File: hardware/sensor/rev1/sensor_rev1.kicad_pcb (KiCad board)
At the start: 2 copper layers, 28.9 x 64.4 mm, 58 parts, among them IC1 STM8L051F3P6, IC2 CC1101RGPR, J1 22-28-4044, J2 M20-9770342, Y1 NX3225GA-26.000M-STD-CRG-2

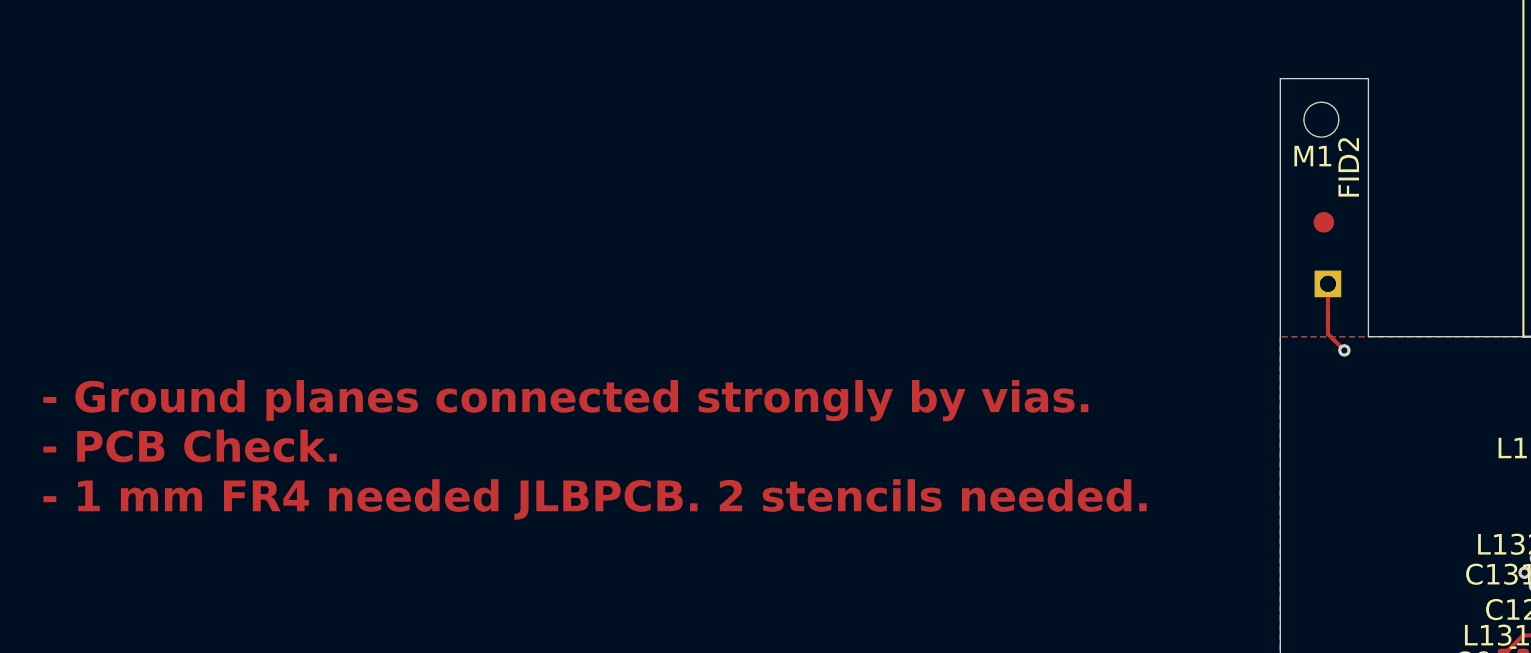
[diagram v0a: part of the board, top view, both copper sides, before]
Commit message: EG-50 Components labels fixed.
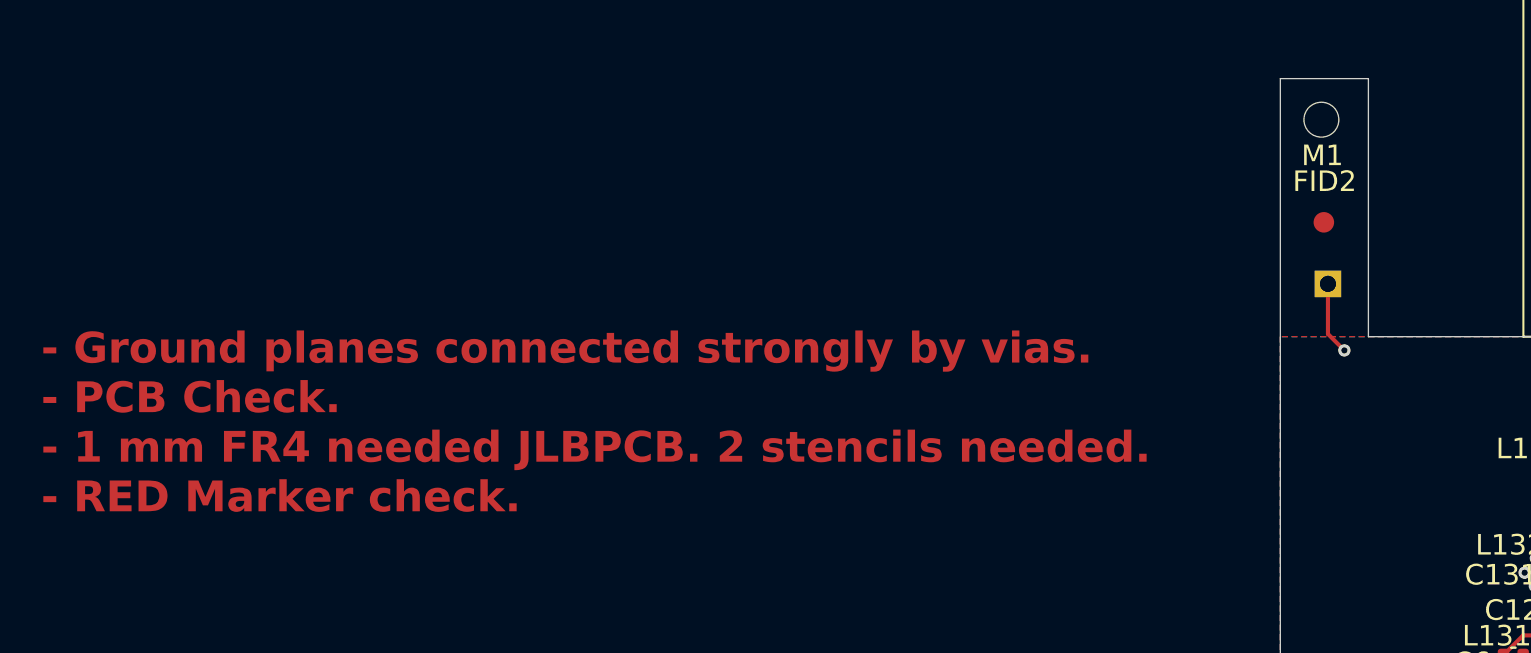
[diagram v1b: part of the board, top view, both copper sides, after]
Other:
- board text added: "- Ground planes connected strongly by vias. - PCB Check. - 1 mm FR4 needed JLBPCB. 2 stencils needed. - RED Marker check."
- board text removed: "- Ground planes connected strongly by vias. - PCB Check. - 1 mm FR4 needed JLBPCB. 2 stencils needed."
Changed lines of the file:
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@@
 		(tags "fiducial")
 		(property "Reference" "FID2"
-			(at 1.25 -2.68 90)
+			(at 0.04 -1.99 180)
 			(layer "F.SilkS")
 			(effects
@@
 		(at 222 92)
 		(property "Reference" "M1"
-			(at -0.42 1.81 0)
+			(at 0.05 1.75 0)
 			(unlocked yes)
 			(layer "F.SilkS")
@@
 		(layer "Edge.Cuts")
 	)
-	(gr_text "- Ground planes connected strongly by vias.\n- PCB Check.\n- 1 mm FR4 needed JLBPCB. 2 stencils needed.\n"
+	(gr_text "- Ground planes connected strongly by vias.\n- PCB Check.\n- 1 mm FR4 needed JLBPCB. 2 stencils needed.\n- RED Marker check.\n"
 		(at 159.63 111.26 0)
 		(layer "F.Cu")
@@
 		(min_thickness 0.25)
 		(filled_areas_thickness no)
-		(fill
+		(fill yes
 			(thermal_gap 0.5)
 			(thermal_bridge_width 0.5)
@@
 		(min_thickness 0.25)
 		(filled_areas_thickness no)
-		(fill
+		(fill yes
 			(thermal_gap 0.5)
 			(thermal_bridge_width 0.5)

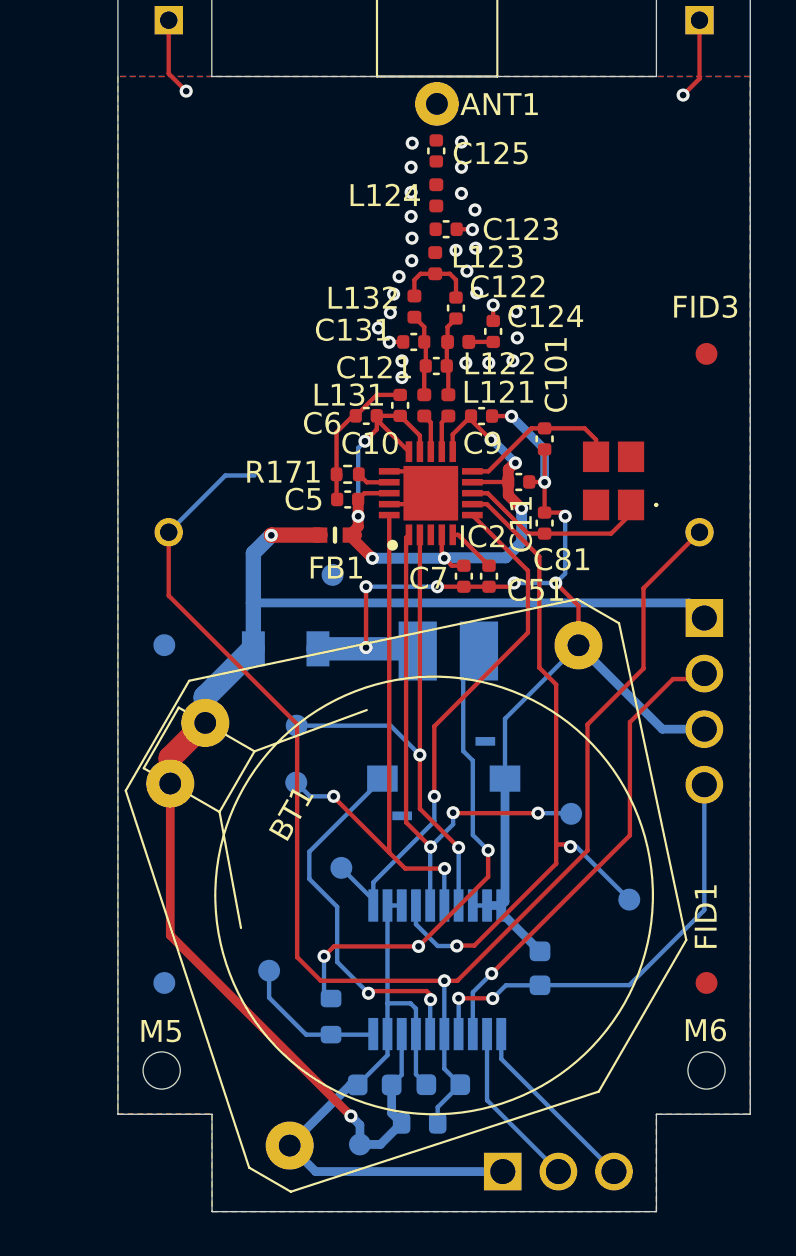
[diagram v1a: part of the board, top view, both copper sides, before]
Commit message: EG-50 Placed vias in the non-RF part.
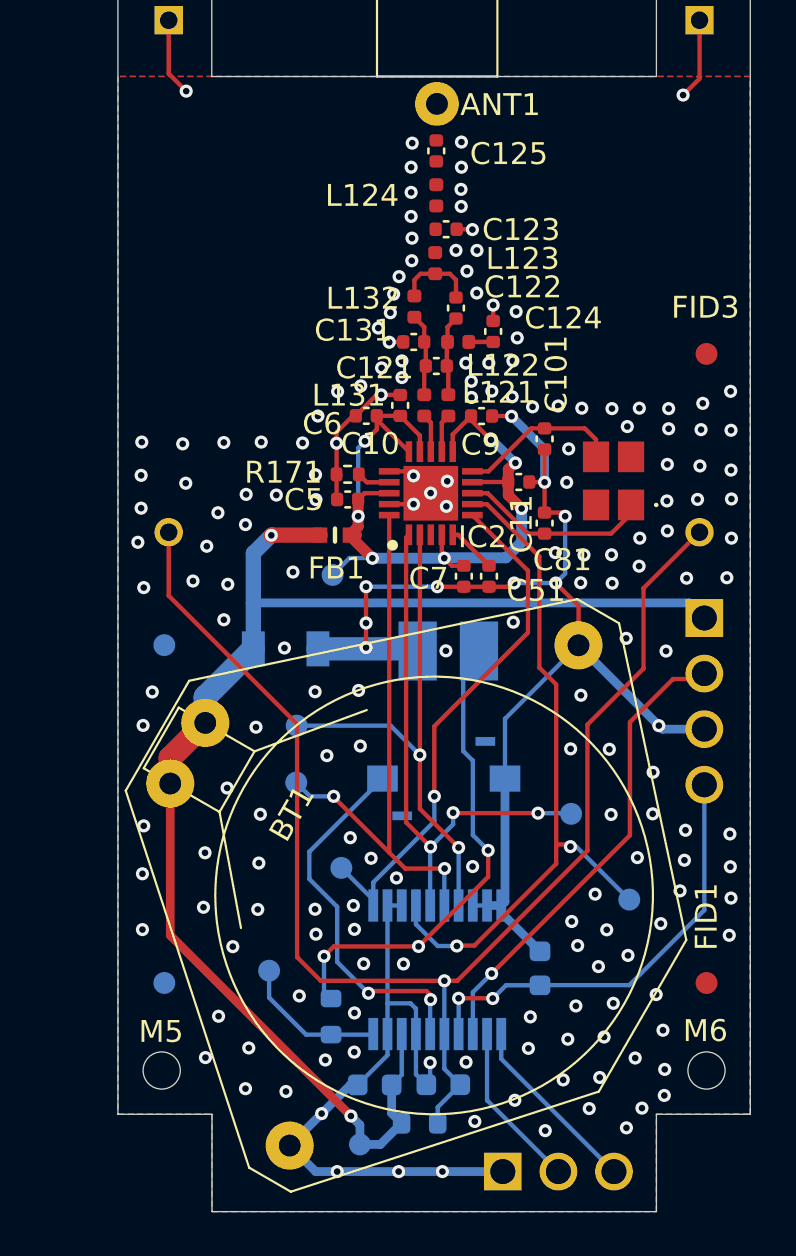
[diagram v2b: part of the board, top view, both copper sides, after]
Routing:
- net REED: track 66.9 -> 61.9 mm
- net RF_VDD: track 35.6 -> 37.8 mm
- net GND: track 108.3 -> 109.4 mm, vias 38 -> 194

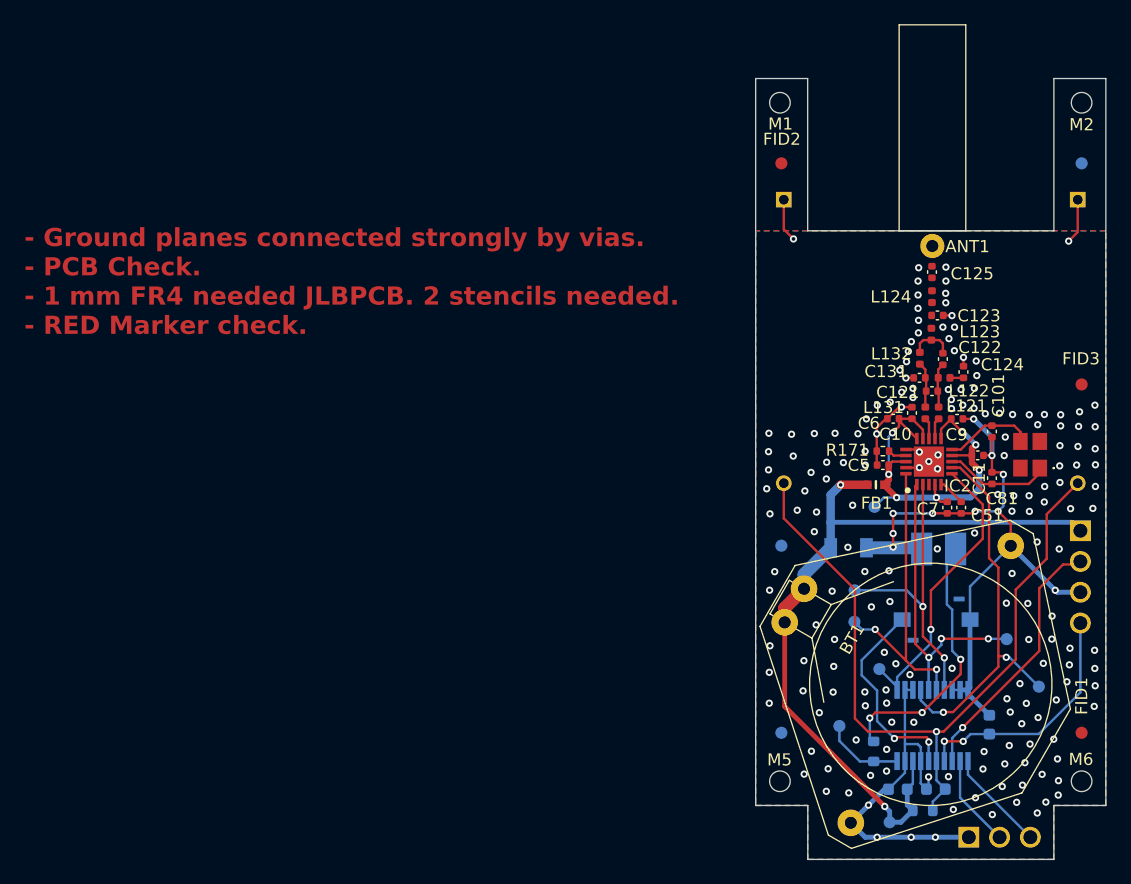
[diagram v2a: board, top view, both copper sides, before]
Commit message: EG-50 DRC errors fixed. Only warnings.
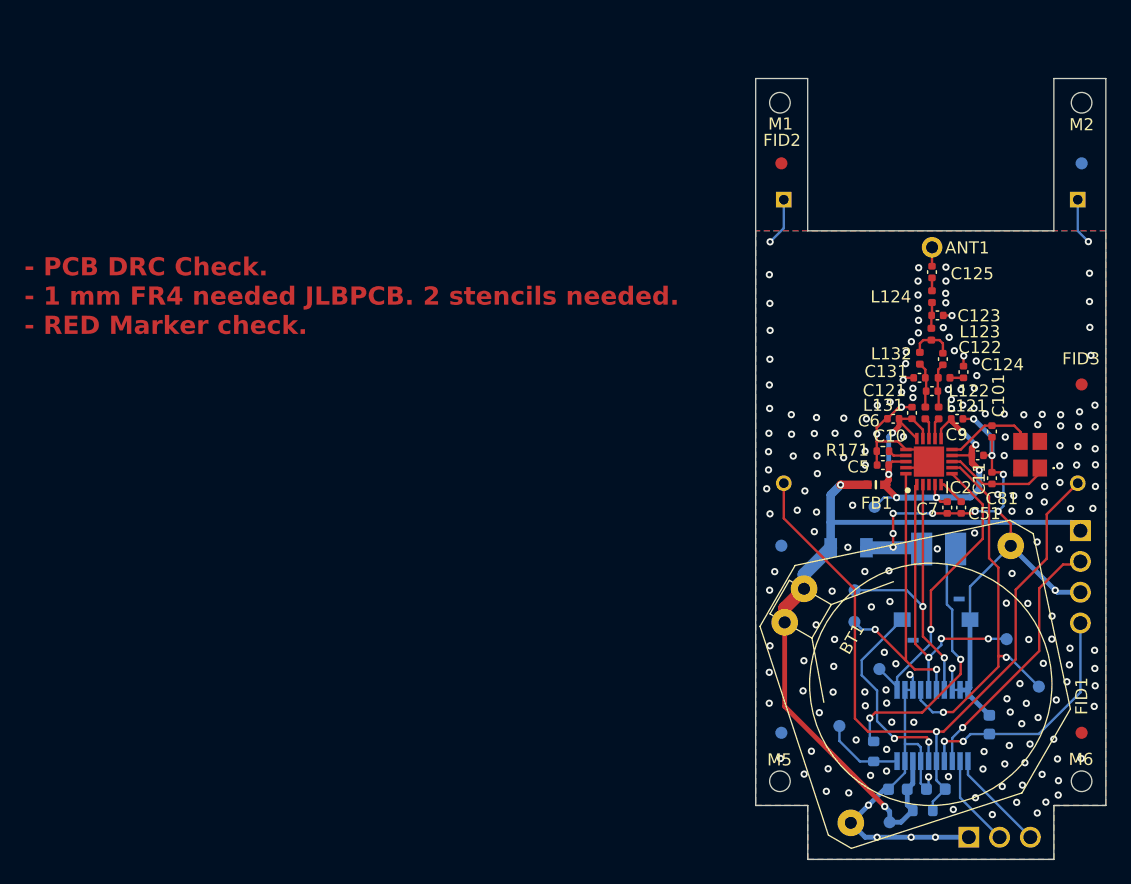
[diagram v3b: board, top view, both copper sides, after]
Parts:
- moved ANT1 0.11 mm to (234.5, 105.7)
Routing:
- net GND: track 109.4 -> 117.5 mm, vias 194 -> 201
- net Net-(C123-Pad2): track 0.00 -> 2.15 mm
- net Net-(ANT1-ANT): track 0.00 -> 1.61 mm
- net Net-(C125-Pad1): track 0.00 -> 1.06 mm
- net Net-(LED1-A): vias 3 -> 2
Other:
- board text added: "- PCB DRC Check. - 1 mm FR4 needed JLBPCB. 2 stencils needed. - RED Marker check."
- board text removed: "- Ground planes connected strongly by vias. - PCB Check. - 1 mm FR4 needed JLBPCB. 2 stencils needed. - RED Marker check."

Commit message: EG-50 Only warings on CR2032 battery holder.
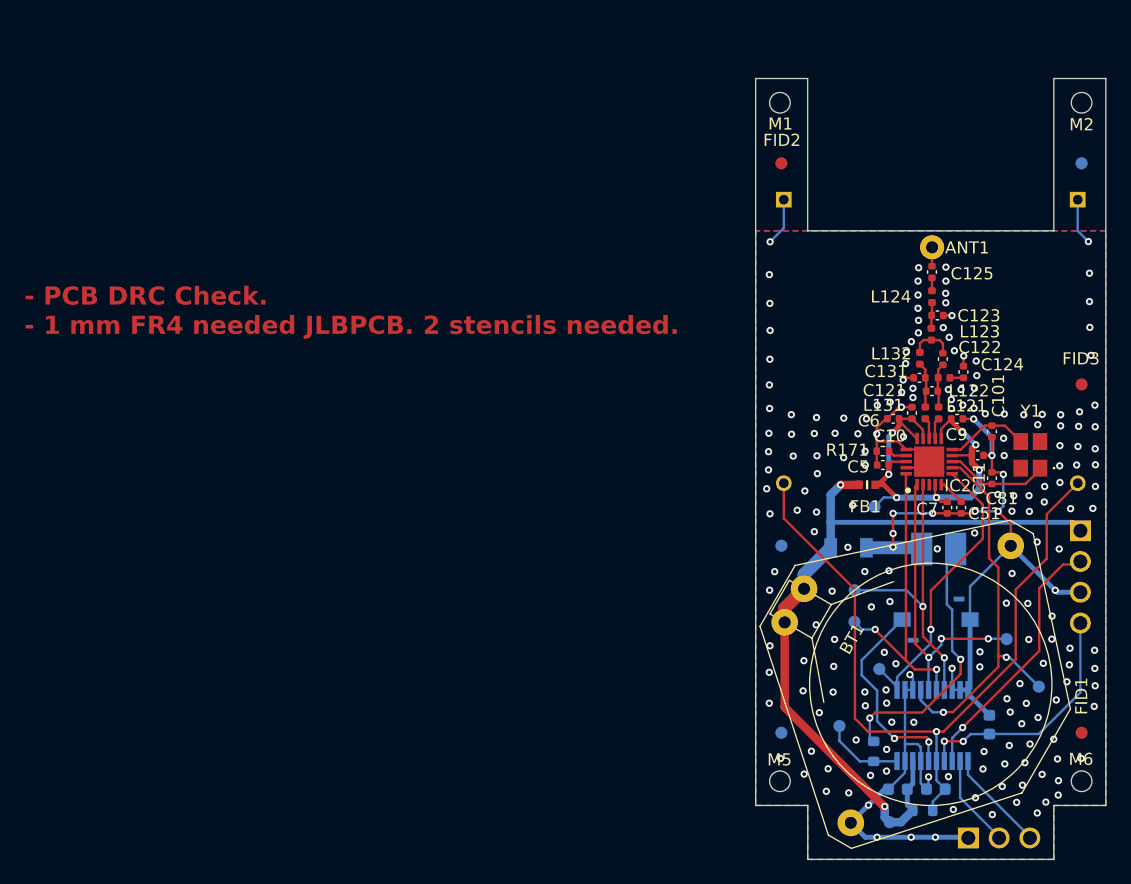
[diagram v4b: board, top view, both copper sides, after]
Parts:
- moved FB1 0.72 mm to (229.2, 123.5), turned to 180 degrees
- moved J2 0.07 mm to (237.6, 152.7)
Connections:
- FB1 pad 1: VDD -> RF_VDD
- FB1 pad 2: RF_VDD -> VDD
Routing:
- net RF_VDD: track 37.8 -> 38.6 mm
- net VDD: track 63.2 -> 62.6 mm
- net GND: vias 201 -> 203
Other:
- board text added: "- PCB DRC Check. - 1 mm FR4 needed JLBPCB. 2 stencils needed."
- board text removed: "- PCB DRC Check. - 1 mm FR4 needed JLBPCB. 2 stencils needed. - RED Marker check."

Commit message: EG-50 Fix the CR2032 battery holder footprint.
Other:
- board text added: "- 1 mm FR4 needed JLBPCB. 2 stencils needed."
- board text removed: "- PCB DRC Check. - 1 mm FR4 needed JLBPCB. 2 stencils needed."
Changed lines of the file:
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@@
 		(fp_line
 			(start -1.6 -14.4)
-			(end -1.6 -14.1)
+			(end -1.6 -14.3)
 			(stroke
 				(width 0.1)
@@
 		(fp_line
 			(start 1.6 -14.4)
-			(end 1.6 -14.1)
+			(end 1.6 -14.3)
 			(stroke
 				(width 0.1)
@@
 		(fp_line
 			(start -1.6 -10.4)
-			(end -1.6 -11.9)
+			(end -1.6 -11.7)
 			(stroke
 				(width 0.1)
@@
 		)
 		(fp_line
-			(start 1.6 -11.9)
+			(start 1.6 -11.7)
 			(end 1.6 -10.4)
 			(stroke
@@
 		)
 		(embedded_fonts no)
-		(model "${KIPRJMOD}/libraries/3dmodels/MyParts/GRM31CR61A107MEA8L.stp"
+		(model "GRM31CR61A107MEA8L.stp"
 			(offset
 				(xyz 0 0 0)
@@
 		)
 		(embedded_fonts no)
+		(model "${KIPRJMOD}/libraries/3dmodels/MyParts/M20-9770342.stp"
+			(offset
+				(xyz 0 0 0)
+			)
+			(scale
+				(xyz 1 1 1)
+			)
+			(rotate
+				(xyz 0 0 0)
+			)
+		)
 	)
 	(footprint "MyParts:PTS636SMG25JSMTRLFS"
@@
 		)
 		(embedded_fonts no)
-		(model "${KIPRJMOD}/libraries/3dmodels/MyParts/PTS636SMG25JSMTR_LFS.stp"
+		(model "PTS636SMG25JSMTR_LFS.stp"
 			(offset
 				(xyz 0 0 0)
@@
 		)
 		(embedded_fonts no)
-		(model "${KIPRJMOD}/libraries/3dmodels/MyParts/VLMS3000-GS08.stp"
+		(model "VLMS3000-GS08.stp"
 			(offset
 				(xyz 0 0 0)
@@
 		)
 		(embedded_fonts no)
-		(model "${KIPRJMOD}/libraries/3dmodels/MyParts/STM8L051F3P6.stp"
+		(model "STM8L051F3P6.stp"
 			(offset
 				(xyz 0 0 0)
@@
 		(layer "Edge.Cuts")
 	)
-	(gr_text "- PCB DRC Check.\n- 1 mm FR4 needed JLBPCB. 2 stencils needed."
+	(gr_text "- 1 mm FR4 needed JLBPCB. 2 stencils needed."
 		(at 159.63 111.26 0)
 		(layer "F.Cu")

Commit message: EG-50 PCB Finalized.
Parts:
- renumbered TP5 to CLK1, TP2 to CS1, TP1 to GD0, TP8 to LED2, TP13 to MCUVDD1, TP3 to MISO1, TP4 to MOSI1, TP14 to RFVDD1
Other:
- board text removed: "- 1 mm FR4 needed JLBPCB. 2 stencils needed."
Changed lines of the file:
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@@
 		)
 		(embedded_fonts no)
-		(model "GP560_20-25.stp"
+		(model "${KIPRJMOD}/libraries/3dmodels/MyParts/GP560_20-25.stp"
 			(offset
-				(xyz 11.72000009 -0.02999999888 3.369999835)
+				(xyz 11.72 -0.03 1.37)
 			)
 			(scale
@@
 			)
 			(rotate
-				(xyz -90 0 0)
+				(xyz -90 -0 -0)
 			)
 		)
@@
 		(descr "SMD pad as test Point, diameter 1.0mm")
 		(tags "test point SMD pad")
-		(property "Reference" "TP4"
-			(at 2.51 0.01 0)
+		(property "Reference" "MOSI1"
+			(at 1.06 -1.88 0)
 			(layer "B.SilkS")
 			(effects
@@
 		)
 		(embedded_fonts no)
-		(model "GRM31CR61A107MEA8L.stp"
+		(model "${KIPRJMOD}/libraries/3dmodels/MyParts/GRM31CR61A107MEA8L.stp"
 			(offset
 				(xyz 0 0 0)
@@
 		)
 		(embedded_fonts no)
-		(model "GP560_20-25.stp"
+		(model "${KIPRJMOD}/libraries/3dmodels/MyParts/GP560_20-25.stp"
 			(offset
-				(xyz 11.72000009 -0.02999999888 3.369999835)
+				(xyz 11.72 -0.03 1.37)
 			)
 			(scale
@@
 			)
 			(rotate
-				(xyz -90 0 0)
+				(xyz -90 -0 -0)
 			)
 		)
@@
 		(descr "SMD pad as test Point, diameter 1.0mm")
 		(tags "test point SMD pad")
-		(property "Reference" "TP2"
+		(property "Reference" "CS1"
 			(at 0.05 1.78 0)
 			(layer "B.SilkS")
@@
 		)
 		(embedded_fonts no)
-		(model "${KIPRJMOD}/libraries/3dmodels/MyParts/M20-9770342.stp"
-			(offset
-				(xyz 0 0 0)
-			)
-			(scale
-				(xyz 1 1 1)
-			)
-			(rotate
-				(xyz 0 0 0)
-			)
-		)
 	)
 	(footprint "MyParts:PTS636SMG25JSMTRLFS"
@@
 		)
 		(embedded_fonts no)
-		(model "PTS636SMG25JSMTR_LFS.stp"
+		(model "${KIPRJMOD}/libraries/3dmodels/MyParts/PTS636SMG25JSMTR_LFS.stp"
 			(offset
 				(xyz 0 0 0)
@@
 		(descr "SMD pad as test Point, diameter 1.0mm")
 		(tags "test point SMD pad")
-		(property "Reference" "TP1"
-			(at 2.38 -0.06 0)
+		(property "Reference" "GD0"
+			(at 2.49 0.01 0)
 			(layer "B.SilkS")
 			(effects
@@
 		(descr "SMD pad as test Point, diameter 1.0mm")
 		(tags "test point SMD pad")
-		(property "Reference" "TP3"
+		(property "Reference" "MISO1"
 			(at 0.43 1.68 0)
 			(layer "B.SilkS")
@@
 		(descr "SMD pad as test Point, diameter 1.0mm")
 		(tags "test point SMD pad")
-		(property "Reference" "TP5"
-			(at -0.26 1.71 0)
+		(property "Reference" "CLK1"
+			(at -0.54 1.8 0)
 			(layer "B.SilkS")
 			(effects
@@
 		(descr "SMD pad as test Point, diameter 1.0mm")
 		(tags "test point SMD pad")
-		(property "Reference" "TP8"
+		(property "Reference" "LED2"
 			(at 0.35 1.73 0)
 			(layer "B.SilkS")
@@
 		(descr "SMD pad as test Point, diameter 1.0mm")
 		(tags "test point SMD pad")
-		(property "Reference" "TP14"
-			(at 2.85 0.02 0)
+		(property "Reference" "RFVDD1"
+			(at 4.03 0.65 0)
 			(layer "B.SilkS")
 			(effects
@@
 		(descr "SMD pad as test Point, diameter 1.0mm")
 		(tags "test point SMD pad")
-		(property "Reference" "TP13"
-			(at 0 -1.81 0)
+		(property "Reference" "MCUVDD1"
+			(at 0.7 -2.05 0)
 			(layer "B.SilkS")
 			(effects
@@
 		)
 		(embedded_fonts no)
-		(model "VLMS3000-GS08.stp"
+		(model "${KIPRJMOD}/libraries/3dmodels/MyParts/VLMS3000-GS08.stp"
 			(offset
 				(xyz 0 0 0)
@@
 		)
 		(embedded_fonts no)
-		(model "STM8L051F3P6.stp"
+		(model "${KIPRJMOD}/libraries/3dmodels/MyParts/STM8L051F3P6.stp"
 			(offset
 				(xyz 0 0 0)
@@
 		(layer "Edge.Cuts")
 	)
-	(gr_text "- 1 mm FR4 needed JLBPCB. 2 stencils needed."
-		(at 159.63 111.26 0)
-		(layer "F.Cu")
-		(effects
-			(font
-				(size 1.5 1.5)
-				(thickness 0.3)
-				(bold yes)
-			)
-			(justify left bottom)
-		)
-	)
 	(gr_text "Exit Guardian - Sensor REV1.0\nNPX4U 2026"
